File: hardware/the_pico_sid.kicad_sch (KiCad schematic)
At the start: 59 parts, among them J1 Conn_01x08, Q1 2N7002, Q2 2N7002, U1 SID_6581, U2 RP2040, U3 W25Q16JVUXIQ, U4 AMS1117-3.3, U5 LM324, U6 74HC245, Y1 12MHz

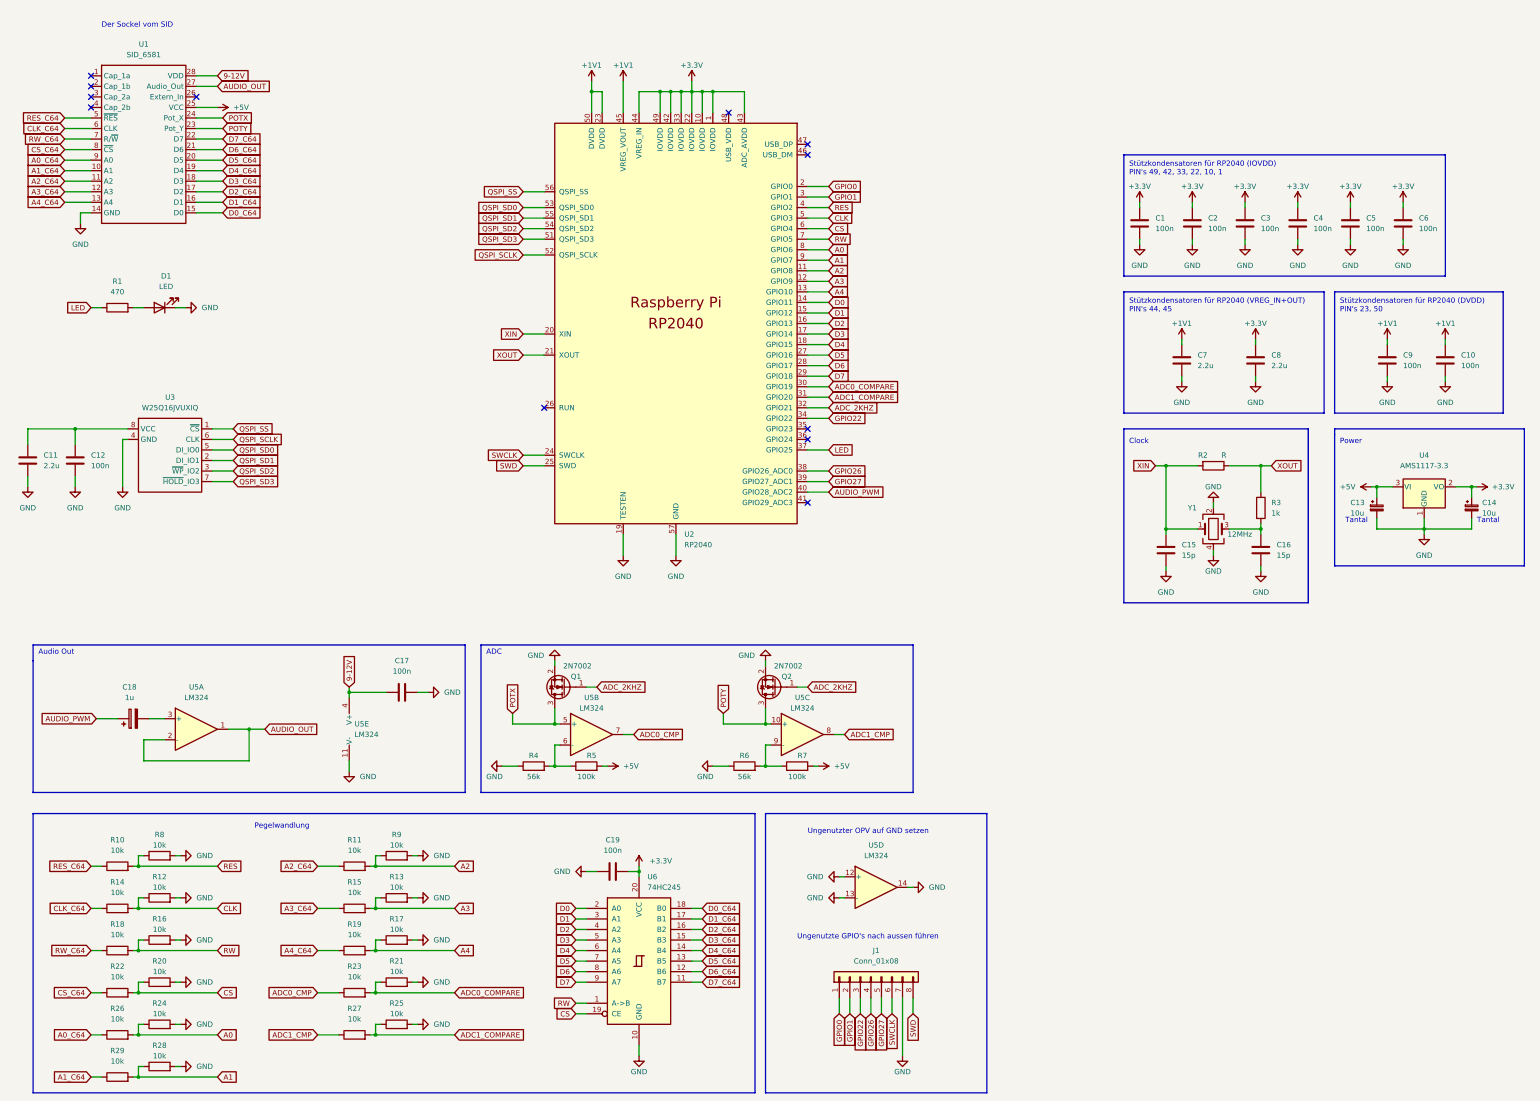
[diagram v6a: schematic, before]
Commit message: shematic: all footprints added
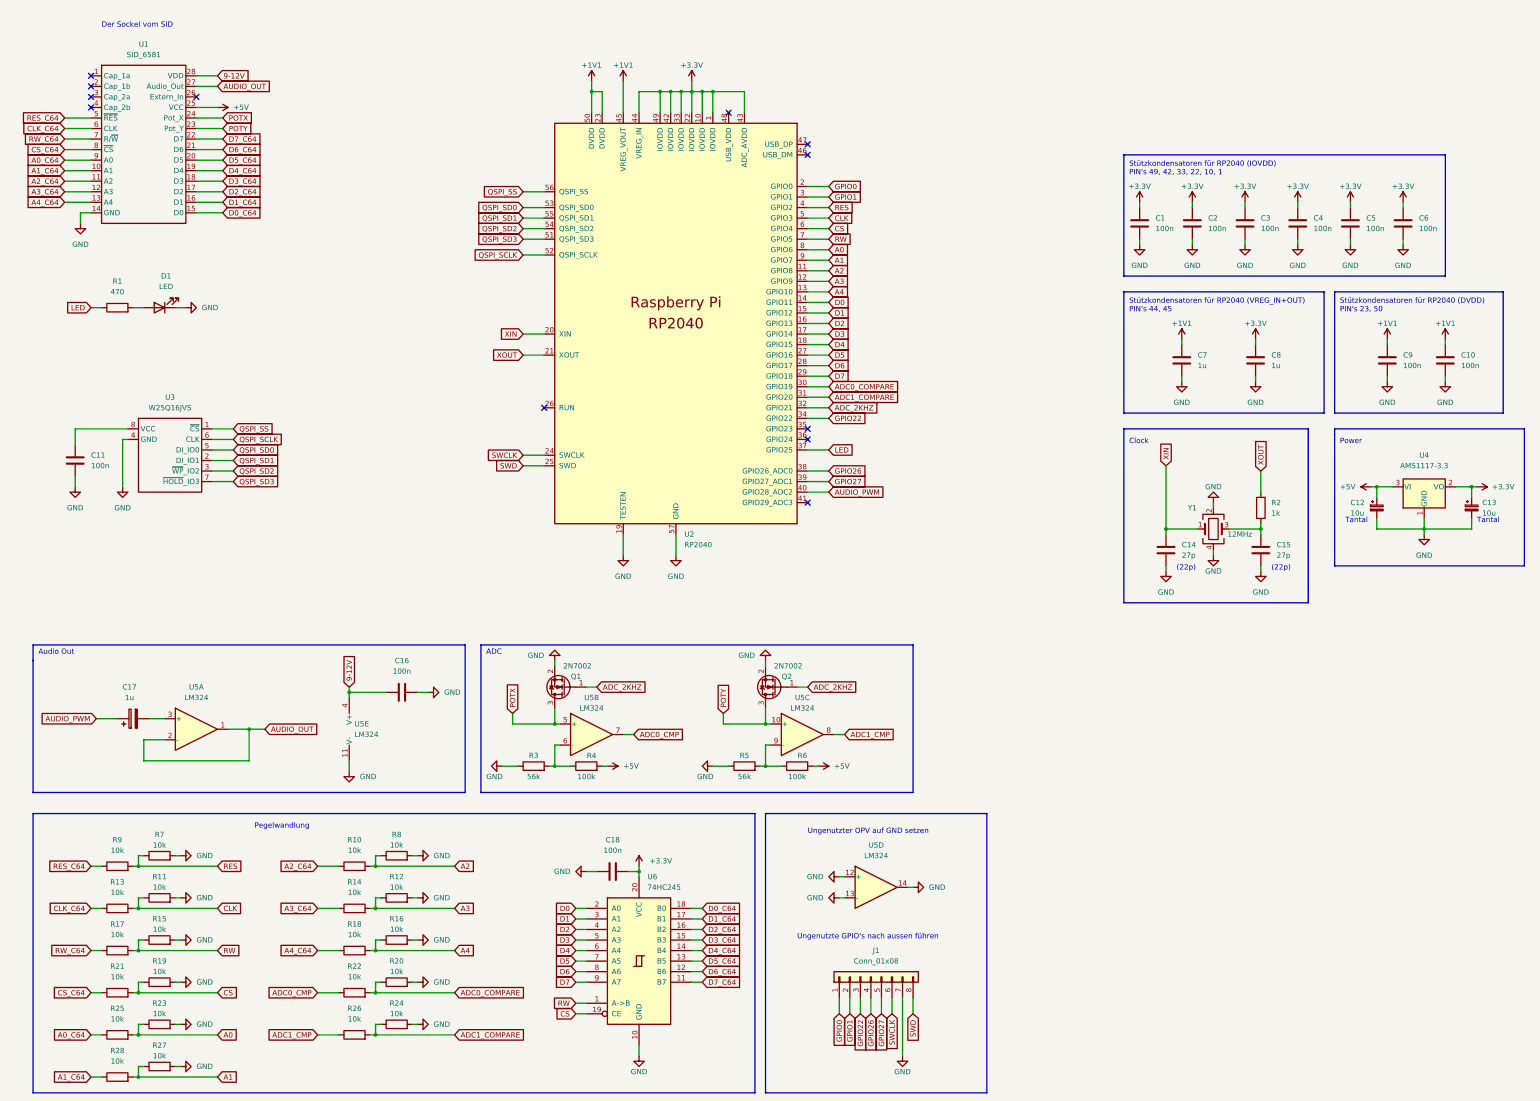
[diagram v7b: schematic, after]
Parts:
- removed C11: 2.2u, Capacitor_SMD:C_0805_2012Metric, symbol Device:C
- removed R2: R, symbol Device:R
- C1, C10, C2, C3, C4, C5, C6, C9: footprint Capacitor_SMD:C_0805_2012Metric -> Capacitor_SMD:C_0603_1608Metric_Pad1.08x0.95mm_HandSolder
- C11: renamed from C12; footprint Capacitor_SMD:C_0805_2012Metric -> Capacitor_SMD:C_0603_1608Metric_Pad1.08x0.95mm_HandSolder
- C12: renamed from C13; footprint (none) -> Capacitor_Tantalum_SMD:CP_EIA-3216-18_Kemet-A_Pad1.58x1.35mm_HandSolder
- C13: renamed from C14; footprint (none) -> Capacitor_Tantalum_SMD:CP_EIA-3216-18_Kemet-A_Pad1.58x1.35mm_HandSolder
- C14: renamed from C15; value 15p -> 27p; footprint Capacitor_SMD:C_0805_2012Metric -> Capacitor_SMD:C_0603_1608Metric_Pad1.08x0.95mm_HandSolder
- C15: renamed from C16; value 15p -> 27p; footprint Capacitor_SMD:C_0805_2012Metric -> Capacitor_SMD:C_0603_1608Metric_Pad1.08x0.95mm_HandSolder
- C16: renamed from C17; footprint Capacitor_SMD:C_0805_2012Metric -> Capacitor_SMD:C_0603_1608Metric_Pad1.08x0.95mm_HandSolder
- C17: renamed from C18; footprint Capacitor_SMD:CP_Elec_4x4.5 -> Capacitor_Tantalum_SMD:CP_EIA-3216-18_Kemet-A_Pad1.58x1.35mm_HandSolder
- C18: renamed from C19; footprint Capacitor_SMD:C_0805_2012Metric -> Capacitor_SMD:C_0603_1608Metric_Pad1.08x0.95mm_HandSolder
- C7, C8: value 2.2u -> 1u; footprint Capacitor_SMD:C_0805_2012Metric -> Capacitor_SMD:C_0603_1608Metric_Pad1.08x0.95mm_HandSolder
- D1: footprint (none) -> LED_SMD:LED_0805_2012Metric_Pad1.15x1.40mm_HandSolder
- J1: footprint (none) -> Connector_PinHeader_2.54mm:PinHeader_1x08_P2.54mm_Vertical
- R1: footprint (none) -> Resistor_SMD:R_0603_1608Metric_Pad0.98x0.95mm_HandSolder
- R10: renamed from R11; footprint (none) -> Resistor_SMD:R_0603_1608Metric_Pad0.98x0.95mm_HandSolder
- R11: renamed from R12; footprint (none) -> Resistor_SMD:R_0603_1608Metric_Pad0.98x0.95mm_HandSolder
- R12: renamed from R13; footprint (none) -> Resistor_SMD:R_0603_1608Metric_Pad0.98x0.95mm_HandSolder
- R13: renamed from R14; footprint (none) -> Resistor_SMD:R_0603_1608Metric_Pad0.98x0.95mm_HandSolder
- R14: renamed from R15; footprint (none) -> Resistor_SMD:R_0603_1608Metric_Pad0.98x0.95mm_HandSolder
- R15: renamed from R16; footprint (none) -> Resistor_SMD:R_0603_1608Metric_Pad0.98x0.95mm_HandSolder
- R16: renamed from R17; footprint (none) -> Resistor_SMD:R_0603_1608Metric_Pad0.98x0.95mm_HandSolder
- R17: renamed from R18; footprint (none) -> Resistor_SMD:R_0603_1608Metric_Pad0.98x0.95mm_HandSolder
- R18: renamed from R19; footprint (none) -> Resistor_SMD:R_0603_1608Metric_Pad0.98x0.95mm_HandSolder
- R19: renamed from R20; footprint (none) -> Resistor_SMD:R_0603_1608Metric_Pad0.98x0.95mm_HandSolder
- R2: renamed from R3; footprint (none) -> Resistor_SMD:R_0603_1608Metric_Pad0.98x0.95mm_HandSolder
- R20: renamed from R21; footprint (none) -> Resistor_SMD:R_0603_1608Metric_Pad0.98x0.95mm_HandSolder
- R21: renamed from R22; footprint (none) -> Resistor_SMD:R_0603_1608Metric_Pad0.98x0.95mm_HandSolder
- R22: renamed from R23; footprint (none) -> Resistor_SMD:R_0603_1608Metric_Pad0.98x0.95mm_HandSolder
- R23: renamed from R24; footprint (none) -> Resistor_SMD:R_0603_1608Metric_Pad0.98x0.95mm_HandSolder
- R24: renamed from R25; footprint (none) -> Resistor_SMD:R_0603_1608Metric_Pad0.98x0.95mm_HandSolder
- R25: renamed from R26; footprint (none) -> Resistor_SMD:R_0603_1608Metric_Pad0.98x0.95mm_HandSolder
- R26: renamed from R27; footprint (none) -> Resistor_SMD:R_0603_1608Metric_Pad0.98x0.95mm_HandSolder
- R27: renamed from R28; footprint (none) -> Resistor_SMD:R_0603_1608Metric_Pad0.98x0.95mm_HandSolder
- R28: renamed from R29; footprint (none) -> Resistor_SMD:R_0603_1608Metric_Pad0.98x0.95mm_HandSolder
- R3: renamed from R4; footprint Resistor_SMD:R_0805_2012Metric -> Resistor_SMD:R_0603_1608Metric_Pad0.98x0.95mm_HandSolder
- R4: renamed from R5; footprint Resistor_SMD:R_0805_2012Metric -> Resistor_SMD:R_0603_1608Metric_Pad0.98x0.95mm_HandSolder
- R5: renamed from R6; footprint Resistor_SMD:R_0805_2012Metric -> Resistor_SMD:R_0603_1608Metric_Pad0.98x0.95mm_HandSolder
- R6: renamed from R7; footprint Resistor_SMD:R_0805_2012Metric -> Resistor_SMD:R_0603_1608Metric_Pad0.98x0.95mm_HandSolder
- R7: renamed from R8; footprint (none) -> Resistor_SMD:R_0603_1608Metric_Pad0.98x0.95mm_HandSolder
- R8: renamed from R9; footprint (none) -> Resistor_SMD:R_0603_1608Metric_Pad0.98x0.95mm_HandSolder
- R9: renamed from R10; footprint (none) -> Resistor_SMD:R_0603_1608Metric_Pad0.98x0.95mm_HandSolder
- U3: value W25Q16JVUXIQ -> W25Q16JVS; footprint Package_SO:SOIC-8W_5.3x5.3mm_P1.27mm -> Package_SO:SO-8_5.3x6.2mm_P1.27mm
- Y1: footprint (none) -> Crystal:Crystal_SMD_EuroQuartz_MJ-4Pin_5.0x3.2mm
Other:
- note added: "(22p)"

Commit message: schematic: added testpoints for usb and boot_sel
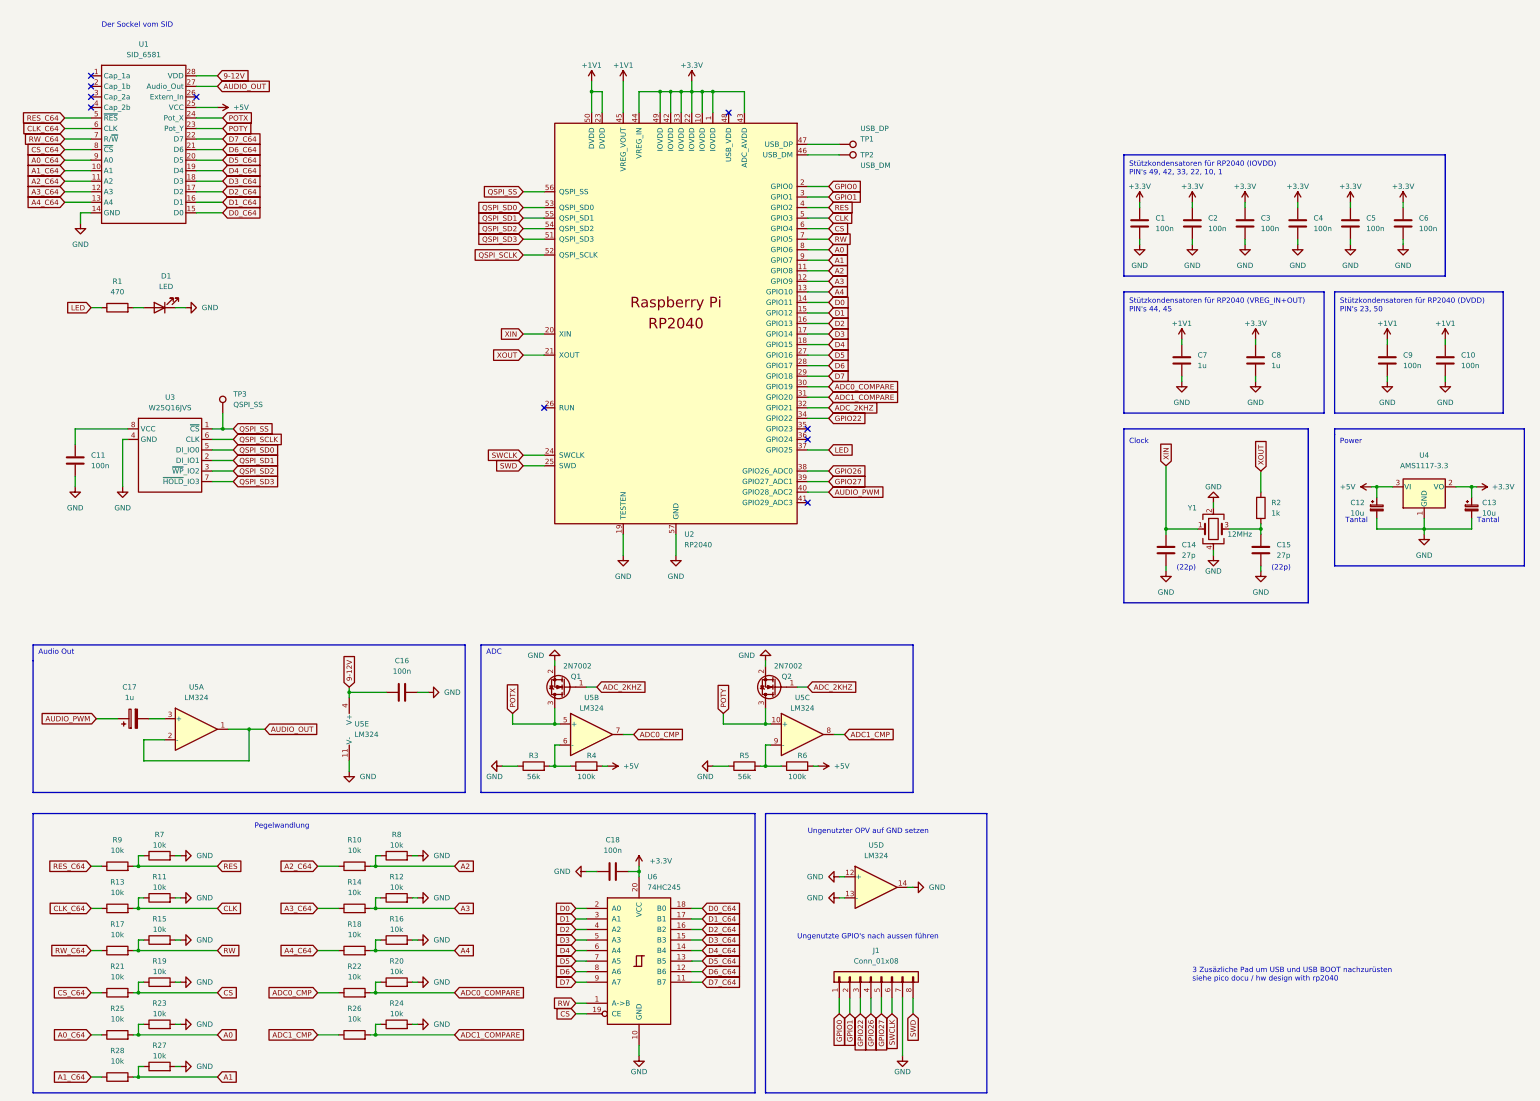
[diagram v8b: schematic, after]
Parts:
- added TP1: USB_DP, TestPoint:TestPoint_Pad_2.5x2.5mm, symbol Connector:TestPoint
- added TP2: USB_DM, TestPoint:TestPoint_Pad_2.5x2.5mm, symbol Connector:TestPoint
- added TP3: QSPI_SS, TestPoint:TestPoint_Pad_2.5x2.5mm, symbol Connector:TestPoint
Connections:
- net QSPI_SS: now also TP3.1
- net at U2.46 (USB_DM): now also TP2.1
- net at U2.47 (USB_DP): now also TP1.1
- no-connect marks 12 -> 10
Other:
- note added: "3 Zusäzliche Pad um USB und USB BOOT nachzurüsten siehe pico docu / hw design with rp2040"
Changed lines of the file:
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@@
   (junction (at 175.26 35.56) (diameter 0) (color 0 0 0 0)
   )
+  (junction (at 67.31 116.84) (diameter 0) (color 0 0 0 0)
+  )
   (junction (at 46.99 273.05) (diameter 0) (color 0 0 0 0)
   )
@@
   (no_connect (at 60.96 36.83))
   (no_connect (at 189.23 40.64))
-  (no_connect (at 208.28 48.26))
   (no_connect (at 208.28 119.38))
   (no_connect (at 35.56 36.83))
@@
   (no_connect (at 208.28 134.62))
   (no_connect (at 208.28 116.84))
-  (no_connect (at 208.28 50.8))
   (wire (pts (xy 208.28 71.12) (xy 213.36 71.12))
     (stroke (width 0) (type default) (color 0 0 0 0))
@@
     (stroke (width 0) (type default) (color 0 0 0 0))
   )
+  (wire (pts (xy 67.31 113.03) (xy 67.31 116.84))
+    (stroke (width 0) (type default) (color 0 0 0 0))
+  )
   (wire (pts (xy 45.72 262.89) (xy 46.99 262.89))
     (stroke (width 0) (type default) (color 0 0 0 0))
@@
     (stroke (width 0) (type default) (color 0 0 0 0))
   )
+  (wire (pts (xy 208.28 50.8) (xy 215.9 50.8))
+    (stroke (width 0) (type default) (color 0 0 0 0))
+  )
   (wire (pts (xy 46.99 242.57) (xy 66.04 242.57))
     (stroke (width 0) (type default) (color 0 0 0 0))
@@
     (stroke (width 0) (type default) (color 0 0 0 0))
   )
+  (wire (pts (xy 208.28 48.26) (xy 215.9 48.26))
+    (stroke (width 0) (type default) (color 0 0 0 0))
+  )
   (wire (pts (xy 364.49 130.81) (xy 368.3 130.81))
     (stroke (width 0) (type default) (color 0 0 0 0))
@@
     (stroke (width 0) (type default) (color 0 0 0 0))
   )
-  (wire (pts (xy 64.77 116.84) (xy 69.85 116.84))
+  (wire (pts (xy 64.77 116.84) (xy 67.31 116.84))
     (stroke (width 0) (type default) (color 0 0 0 0))
   )
@@
     (stroke (width 0) (type default) (color 0 0 0 0))
   )
+  (wire (pts (xy 67.31 116.84) (xy 69.85 116.84))
+    (stroke (width 0) (type default) (color 0 0 0 0))
+  )
   (wire (pts (xy 313.69 62.23) (xy 313.69 63.5))
     (stroke (width 0) (type default) (color 0 0 0 0))
@@
     (effects (font (size 1.27 1.27)) (justify left bottom))
   )
+  (text "3 Zusäzliche Pad um USB und USB BOOT nachzurüsten\nsiehe pico docu / hw design with rp2040"
+    (at 300.99 250.19 0)
+    (effects (font (size 1.27 1.27)) (justify left bottom))
+  )
   (text "Ungenutzte GPIO's nach aussen führen" (at 205.74 240.03 0)
     (effects (font (size 1.27 1.27)) (justify left bottom))
@@
     (pin "1")
   )
+  (symbol (lib_id "Connector:TestPoint") (at 215.9 50.8 270) (unit 1)
+    (in_bom yes) (on_board yes)
+    (property "Reference" "TP2" (id 0) (at 220.98 50.8 90)
+      (effects (font (size 1.27 1.27)) (justify left))
+    )
+    (property "Value" "USB_DM" (id 1) (at 220.98 53.34 90)
+      (effects (font (size 1.27 1.27)) (justify left))
+    )
+    (property "Footprint" "TestPoint:TestPoint_Pad_2.5x2.5mm" (id 2) (at 215.9 55.88 0)
+      (effects (font (size 1.27 1.27)) hide)
+    )
+    (property "Datasheet" "~" (id 3) (at 215.9 55.88 0)
+      (effects (font (size 1.27 1.27)) hide)
+    )
+    (pin "1")
+  )
   (symbol (lib_id "power:GND") (at 317.5 151.13 0) (unit 1)
     (in_bom yes) (on_board yes) (fields_autoplaced)
@@
     (pin "2")
   )
+  (symbol (lib_id "Connector:TestPoint") (at 215.9 48.26 270) (unit 1)
+    (in_bom yes) (on_board yes)
+    (property "Reference" "TP1" (id 0) (at 220.98 46.9899 90)
+      (effects (font (size 1.27 1.27)) (justify left))
+    )
+    (property "Value" "USB_DP" (id 1) (at 220.98 44.45 90)
+      (effects (font (size 1.27 1.27)) (justify left))
+    )
+    (property "Footprint" "TestPoint:TestPoint_Pad_2.5x2.5mm" (id 2) (at 215.9 53.34 0)
+      (effects (font (size 1.27 1.27)) hide)
+    )
+    (property "Datasheet" "~" (id 3) (at 215.9 53.34 0)
+      (effects (font (size 1.27 1.27)) hide)
+    )
+    (pin "1")
+  )
   (symbol (lib_id "power:GND") (at 114.3 240.03 90) (unit 1)
     (in_bom yes) (on_board yes) (fields_autoplaced)
@@
     (pin "1")
   )
+  (symbol (lib_id "Connector:TestPoint") (at 67.31 113.03 0) (unit 1)
+    (in_bom yes) (on_board yes) (fields_autoplaced)
+    (property "Reference" "TP3" (id 0) (at 69.85 108.4579 0)
+      (effects (font (size 1.27 1.27)) (justify left))
+    )
+    (property "Value" "QSPI_SS" (id 1) (at 69.85 110.9979 0)
+      (effects (font (size 1.27 1.27)) (justify left))
+    )
+    (property "Footprint" "TestPoint:TestPoint_Pad_2.5x2.5mm" (id 2) (at 72.39 113.03 0)
+      (effects (font (size 1.27 1.27)) hide)
+    )
+    (property "Datasheet" "~" (id 3) (at 72.39 113.03 0)
+      (effects (font (size 1.27 1.27)) hide)
+    )
+    (pin "1")
+  )
   (symbol (lib_id "c64_tk:SID_6581") (at 48.26 48.26 0) (unit 1)
     (in_bom yes) (on_board yes) (fields_autoplaced)
@@
       (reference "R28") (unit 1) (value "10k") (footprint "Resistor_SMD:R_0603_1608Metric_Pad0.98x0.95mm_HandSolder")
     )
+    (path "/8f78d29a-6df7-4316-b687-8254e9fd2f96"
+      (reference "TP1") (unit 1) (value "USB_DP") (footprint "TestPoint:TestPoint_Pad_2.5x2.5mm")
+    )
+    (path "/25c69ac2-e40b-4ba7-b4aa-0db5cb950dd8"
+      (reference "TP2") (unit 1) (value "USB_DM") (footprint "TestPoint:TestPoint_Pad_2.5x2.5mm")
+    )
+    (path "/dcabffed-ea54-40b1-97af-ea653625c295"
+      (reference "TP3") (unit 1) (value "QSPI_SS") (footprint "TestPoint:TestPoint_Pad_2.5x2.5mm")
+    )
     (path "/dd6bc294-7c40-41ff-a436-ec7f5ef2ef0c"
